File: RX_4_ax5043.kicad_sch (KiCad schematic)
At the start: 23 parts, among them U501 RFShield_OnePiece, U505 AX5043, U506 TPS22919D

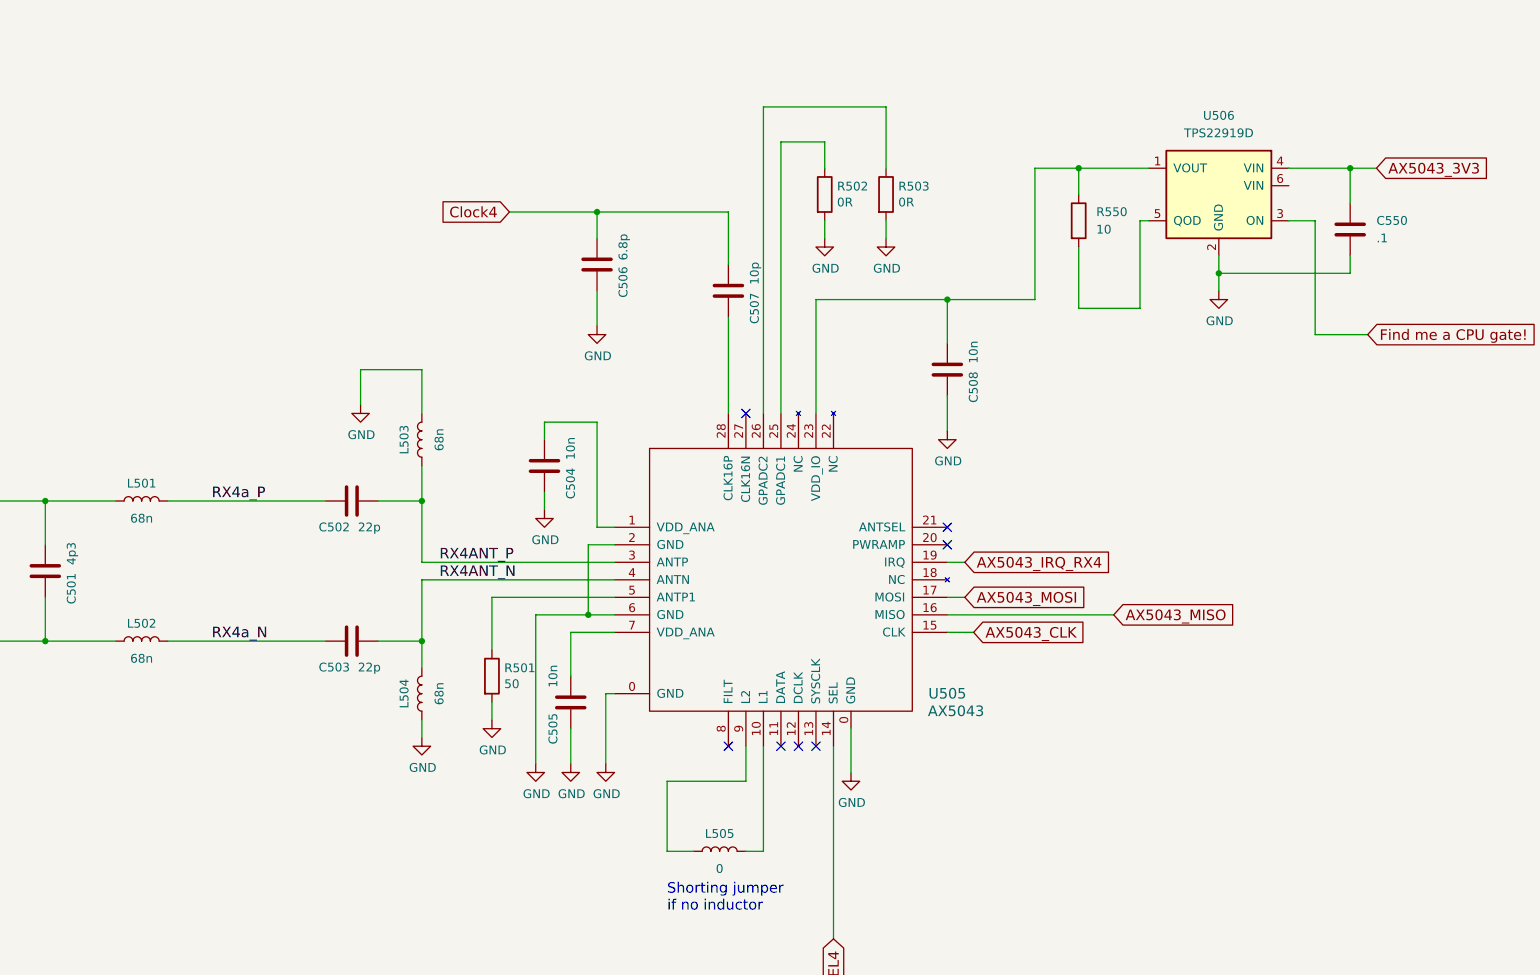
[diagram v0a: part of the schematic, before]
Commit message: Lots of cleanups to fix numerous issues
Signed-off-by: Corey Minyard <corey@minyard.net>
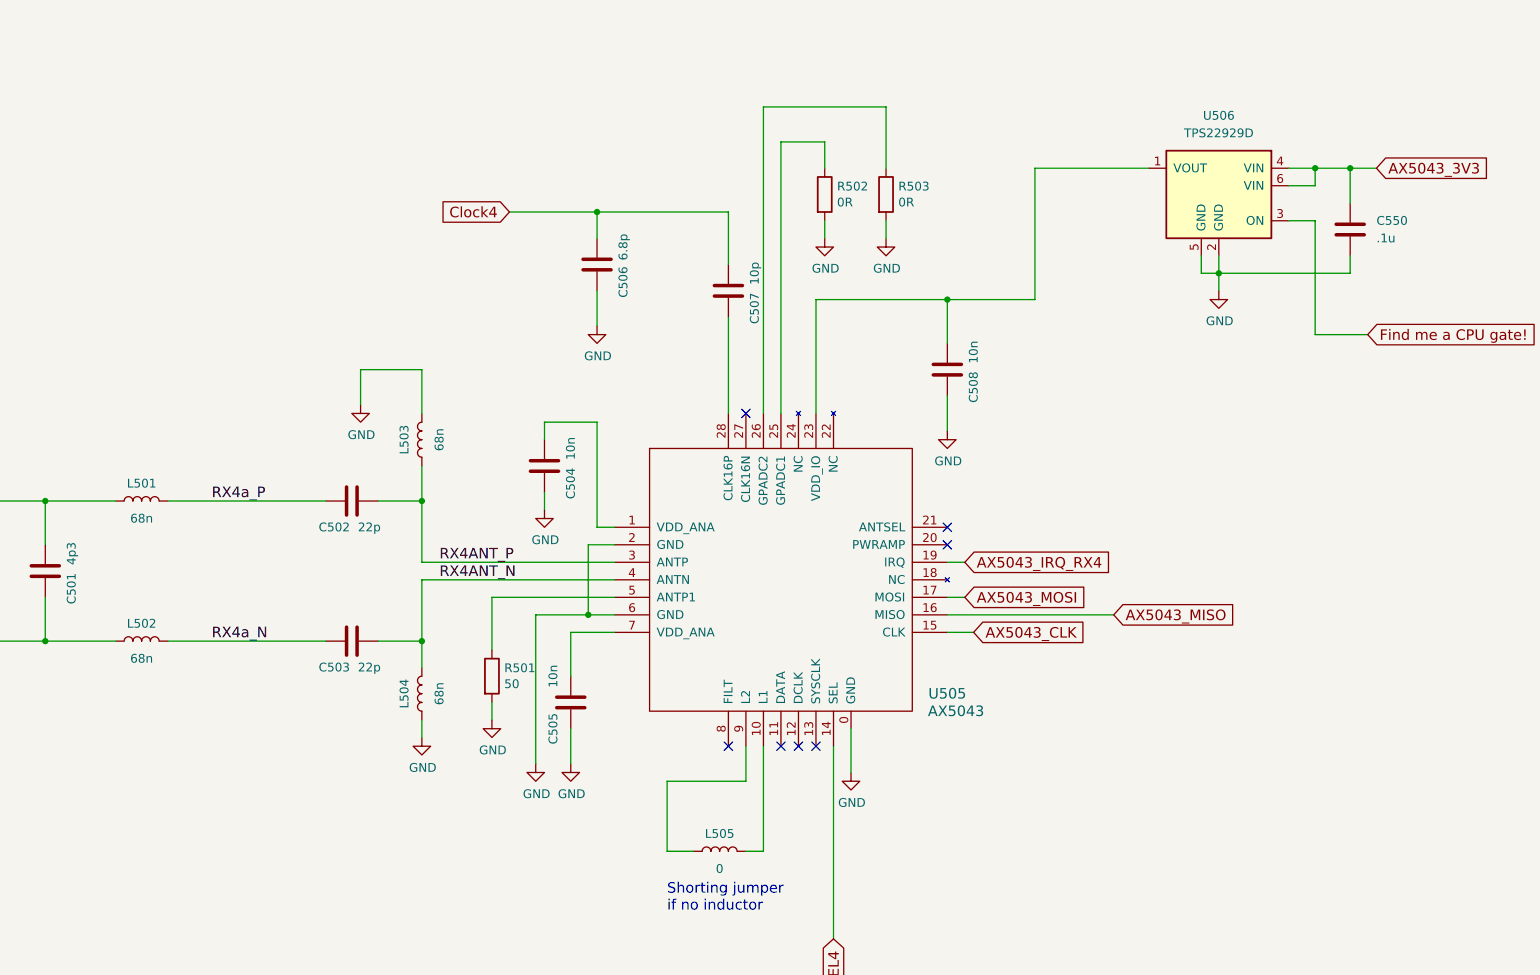
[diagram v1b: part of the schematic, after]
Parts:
- removed R550: 10, symbol Device:R
- C550: value .1 -> .1u; footprint (none) -> Capacitor_SMD:C_0402_1005Metric
- U506: value TPS22919D -> TPS22929D
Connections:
- net AX5043_3V3: now also U506.6 (VIN)
- net GND: now also U506.5 (GND)

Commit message: Start ripping things apart
Signed-off-by: Corey Minyard <corey@minyard.net>
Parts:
- removed C501: 4p3, Capacitor_SMD:C_0603_1608Metric_Pad1.08x0.95mm_HandSolder, symbol Device:C
- removed C502, C503: 22p, Capacitor_SMD:C_0603_1608Metric_Pad1.08x0.95mm_HandSolder, symbol Device:C
- removed L501, L502, L503, L504: 68n, PacSatDev_misc:L_Murata_LQH2MCNxxxx02_2.0x1.6mm, symbol Device:L
- removed P502: ~, PacSatDev_misc:U_FL, symbol PACSAT_DEV_misc:U_FL
- added L92: WBC1-1TL, IND6_WBC1, symbol PACSAT_DEV_misc:WBC1-1TL
- added R101: 10K, Resistor_SMD:R_0603_1608Metric_Pad0.98x0.95mm_HandSolder, symbol Device:R
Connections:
- net GND: now also L92.2, L92.4, R101.2
- net RX4ANT_N: now also L92.3
- net RX4ANT_P: now also L92.1
- net Find me a CPU gate! renamed AX5043_EN_RX4
- net AX5043_EN_RX4: now also R101.1
- net RX4b_P: no longer names the net of P501.1 (In)
- net RX4b_P: now also L92.6
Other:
- note removed: "Rx4-"
- moved on the sheet: P501

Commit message: More hacking on things
Signed-off-by: Corey Minyard <corey@minyard.net>
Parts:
- removed U501: RFShield_OnePiece, PacSatDev_misc:RF_SHIELD_BMI_S_202_F_U501, symbol PACSAT_DEV_misc:RF_SHIELD_BOX

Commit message: Clean up RTC, start working on power
Signed-off-by: Corey Minyard <corey@minyard.net>
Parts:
- L92: footprint IND6_WBC1 -> PacSatDev_misc:IND6_WBC1
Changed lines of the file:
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@@
 			)
 		)
-		(property "Footprint" "IND6_WBC1"
+		(property "Footprint" "PacSatDev_misc:IND6_WBC1"
 			(at 158.75 125.73 0)
 			(effects

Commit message: Finish up most of the ax5043 routing
Signed-off-by: Corey Minyard <corey@minyard.net>
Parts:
- L505: footprint PacSatDev_misc:L_Murata_LQH2MCNxxxx02_2.0x1.6mm -> Inductor_SMD:L_0603_1608Metric_Pad1.05x0.95mm_HandSolder
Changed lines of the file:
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@@
 			)
 		)
-		(property "Footprint" "PacSatDev_misc:L_Murata_LQH2MCNxxxx02_2.0x1.6mm"
+		(property "Footprint" "Inductor_SMD:L_0603_1608Metric_Pad1.05x0.95mm_HandSolder"
 			(at 208.28 171.45 0)
 			(effects

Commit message: Do a lot of routing work
RX input is done, 5043s are done, power is done.

Signed-off-by: Corey Minyard <corey@minyard.net>
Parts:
- added R122: 0R, Resistor_SMD:R_0603_1608Metric_Pad0.98x0.95mm_HandSolder, symbol Device:R
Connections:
- net at L92.6, P501.1 (In): now also R122.2
- new net Port4_P: R122.1
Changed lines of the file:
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@@
+	)
+	(junction
+		(at 119.38 125.73)
+		(diameter 0)
+		(color 0 0 0 0)
 	)
 	(junction
@@
 	(wire
 		(pts
+			(xy 119.38 125.73) (xy 128.27 125.73)
+		)
+		(stroke
+			(width 0)
+			(type default)
+		)
+	)
+	(wire
+		(pts
 			(xy 241.3 91.44) (xy 254 91.44)
 		)
@@
 	(wire
 		(pts
+			(xy 119.38 120.65) (xy 119.38 125.73)
+		)
+		(stroke
+			(width 0)
+			(type default)
+		)
+	)
+	(wire
+		(pts
 			(xy 158.75 130.81) (xy 161.29 130.81)
 		)
@@
 	(wire
 		(pts
-			(xy 113.03 125.73) (xy 128.27 125.73)
+			(xy 113.03 125.73) (xy 119.38 125.73)
 		)
 		(stroke
@@
 		(pts
 			(xy 193.04 139.7) (xy 186.69 139.7)
+		)
+		(stroke
+			(width 0)
+			(type default)
+		)
+	)
+	(wire
+		(pts
+			(xy 119.38 104.14) (xy 119.38 113.03)
 		)
 		(stroke
@@
 				)
 				(justify right)
+				(hide yes)
+			)
+		)
+	)
+	(global_label "Port4_P"
+		(shape input)
+		(at 119.38 104.14 90)
+		(fields_autoplaced yes)
+		(effects
+			(font
+				(size 1.524 1.524)
+			)
+			(justify left)
+		)
+		(property "Intersheetrefs" "${INTERSHEET_REFS}"
+			(at 119.38 92.4895 90)
+			(effects
+				(font
+					(size 1.27 1.27)
+				)
+				(justify left)
 				(hide yes)
 			)
@@
 					(unit 1)
 				)
+			)
+		)
+	)
+	(symbol
+		(lib_id "Device:R")
+		(at 119.38 116.84 0)
+		(unit 1)
+		(exclude_from_sim no)
+		(in_bom yes)
+		(on_board yes)
+		(dnp no)
+		(property "Reference" "R122"
+			(at 121.158 115.6716 0)
+			(effects
+				(font
+					(size 1.27 1.27)
+				)
+				(justify left)
+			)
+		)
+		(property "Value" "0R"
+			(at 121.158 117.983 0)
+			(effects
+				(font
+					(size 1.27 1.27)
+				)
+				(justify left)
+			)
+		)
+		(property "Footprint" "Resistor_SMD:R_0603_1608Metric_Pad0.98x0.95mm_HandSolder"
+			(at 117.602 116.84 90)
+			(effects
+				(font
+					(size 1.27 1.27)
+				)
+				(hide yes)
+			)
+		)
+		(property "Datasheet" "~"
+			(at 119.38 116.84 0)
+			(effects
+				(font
+					(size 1.27 1.27)
+				)
+			)
+		)
+		(property "Description" ""
+			(at 119.38 116.84 0)
+			(effects
+				(font
+					(size 1.27 1.27)
+				)
+			)
+		)
+		(pin "1"
+		)
+		(pin "2"
+		)
+		(instances
+			(project "PacSat_AFSK"
+				(path "/cc9f42d2-6985-41ac-acab-5ab7b01c5b38/f99c6a69-4136-42a1-b9ff-80c66d5e136e"
+					(reference "R122")
+					(unit 1)
+				)

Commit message: Wire in clocks, more cleanups, wire in MRAM
Signed-off-by: Corey Minyard <corey@minyard.net>
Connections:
- net Clock4 renamed Clock_RX4
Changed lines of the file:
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@@
 		)
 	)
-	(global_label "Clock4"
+	(global_label "Clock_RX4"
 		(shape input)
 		(at 177.8 78.74 180)
@@
 		)
 		(property "Intersheetrefs" "${INTERSHEET_REFS}"
-			(at 167.406 78.74 0)
+			(at 163.1741 78.74 0)
 			(effects
 				(font

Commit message: Finish up and clean up a lot of things
Signed-off-by: Corey Minyard <corey@minyard.net>
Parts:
- added R130: 1K, Resistor_SMD:R_0603_1608Metric_Pad0.98x0.95mm_HandSolder, symbol Device:R
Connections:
- net AX5043_CLK: now also R130.2; no longer U505.15 (CLK)
- new net: R130.1, U505.15 (CLK)
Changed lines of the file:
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@@
+	(wire
+		(pts
+			(xy 257.81 139.7) (xy 265.43 139.7)
+		)
+		(stroke
+			(width 0)
+			(type default)
+		)
+	)
 	(wire
 		(pts
@@
 	(wire
 		(pts
-			(xy 241.3 139.7) (xy 245.11 139.7)
+			(xy 241.3 139.7) (xy 250.19 139.7)
 		)
 		(stroke
@@
 	(global_label "AX5043_CLK"
 		(shape input)
-		(at 245.11 139.7 0)
+		(at 265.43 139.7 0)
 		(fields_autoplaced yes)
 		(effects
@@
 		)
 		(property "Intersheetrefs" "${INTERSHEET_REFS}"
-			(at 261.8175 139.7 0)
+			(at 282.1375 139.7 0)
 			(effects
 				(font
@@
 					(unit 1)
 				)
+			)
+		)
+	)
+	(symbol
+		(lib_id "Device:R")
+		(at 254 139.7 90)
+		(unit 1)
+		(exclude_from_sim no)
+		(in_bom yes)
+		(on_board yes)
+		(dnp no)
+		(property "Reference" "R130"
+			(at 254.254 141.986 90)
+			(effects
+				(font
+					(size 1.27 1.27)
+				)
+			)
+		)
+		(property "Value" "1K"
+			(at 254.254 144.526 90)
+			(effects
+				(font
+					(size 1.27 1.27)
+				)
+			)
+		)
+		(property "Footprint" "Resistor_SMD:R_0603_1608Metric_Pad0.98x0.95mm_HandSolder"
+			(at 254 141.478 90)
+			(effects
+				(font
+					(size 1.27 1.27)
+				)
+				(hide yes)
+			)
+		)
+		(property "Datasheet" "~"
+			(at 254 139.7 0)
+			(effects
+				(font
+					(size 1.27 1.27)
+				)
+				(hide yes)
+			)
+		)
+		(property "Description" "Resistor"
+			(at 254 139.7 0)
+			(effects
+				(font
+					(size 1.27 1.27)
+				)
+				(hide yes)
+			)
+		)
+		(pin "1"
+		)
+		(pin "2"
+		)
+		(instances
+			(project "PacSat_AFSK"
+				(path "/cc9f42d2-6985-41ac-acab-5ab7b01c5b38/f99c6a69-4136-42a1-b9ff-80c66d5e136e"
+					(reference "R130")
+					(unit 1)
+				)
